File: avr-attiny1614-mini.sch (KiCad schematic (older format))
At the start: 15 parts, among them J1 Conn_01x05, J2 Conn_01x07, J3 BAT_JST_PH, Q1 Q_PMOS_GSD, SW1 SW_SPST, U1 attiny1614

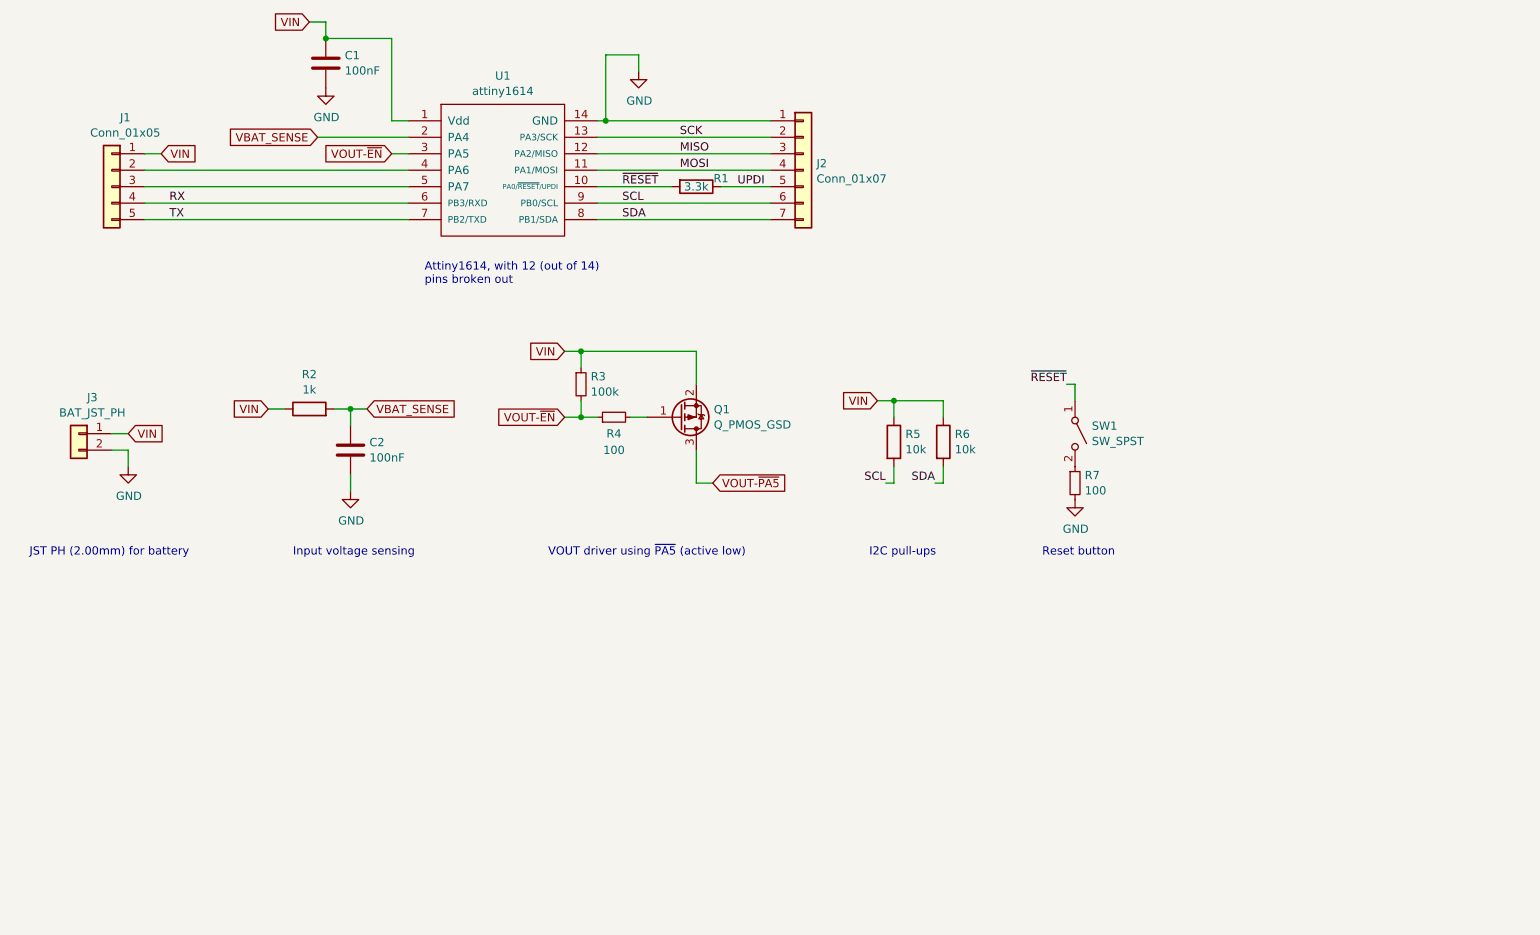
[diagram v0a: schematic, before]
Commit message: Remove VSENSE. Add EXT_LOAD driver.
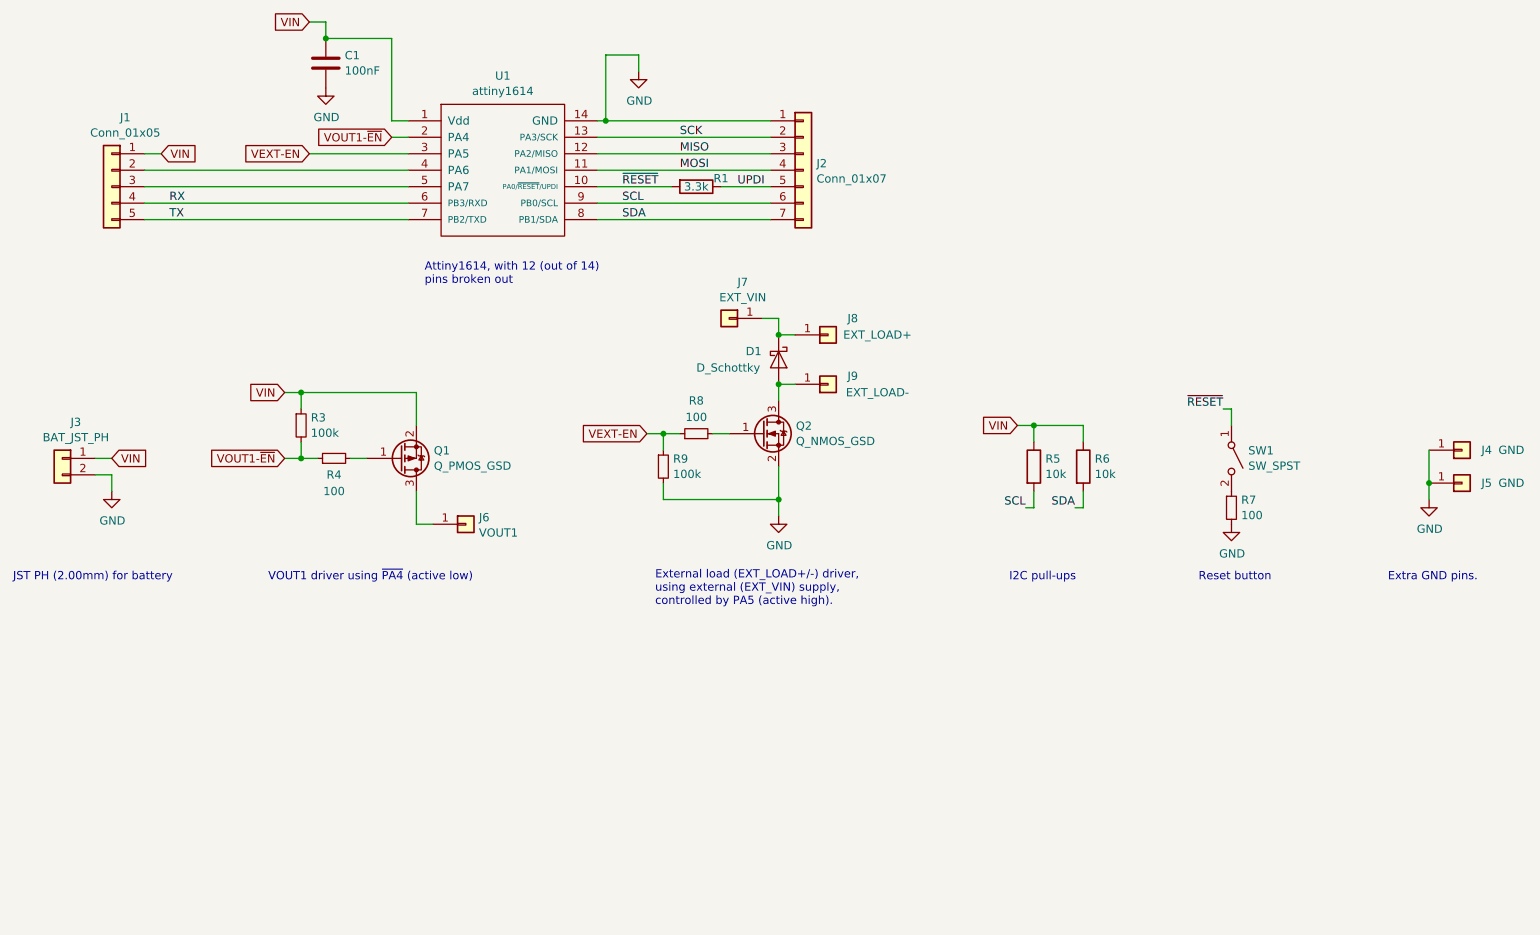
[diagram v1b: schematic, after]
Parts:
- removed C2: 100nF, local_footprints:0805_HS, symbol Device:C
- removed R2: 1k, local_footprints:0805_HS, symbol Device:R
- added D1: D_Schottky, local_footprints:1206_HS, symbol Device:D_Schottky
- added J4, J5: GND, local_footprints:Pin_Header_Straight_1x01_Pitch2.54mm, symbol Connector_Generic:Conn_01x01
- added J6: VOUT1, local_footprints:Pin_Header_Straight_1x01_Pitch2.54mm, symbol Connector_Generic:Conn_01x01
- added J7: EXT_VIN, local_footprints:Pin_Header_Straight_1x01_Pitch2.54mm, symbol Connector_Generic:Conn_01x01
- added J8: EXT_LOAD+, local_footprints:Pin_Header_Straight_1x01_Pitch2.54mm, symbol Connector_Generic:Conn_01x01
- added J9: EXT_LOAD-, local_footprints:Pin_Header_Straight_1x01_Pitch2.54mm, symbol Connector_Generic:Conn_01x01
- added Q2: Q_NMOS_GSD, local_footprints:SOT-23_HS, symbol Device:Q_NMOS_GSD
- added R8: 100, local_footprints:1206_HS, symbol Device:R_Small
- added R9: 100k, local_footprints:0805_HS, symbol Device:R_Small
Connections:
- net GND: now also J4.1 (Pin_1), J5.1 (Pin_1), Q2.2 (S), R9.2
- net VBAT_SENSE renamed VOUT1-~EN
- net VOUT1-~EN: now also R3.2, R4.1
- removed net VOUT-~EN: R3.2, R4.1, U1.3 (PA5)
- net VOUT-~PA5: no longer names the net of Q1.3 (D)
- net VOUT-~PA5: now also J6.1 (Pin_1)
- new net: Q2.1 (G), R8.2
- new net: D1.2 (A), J9.1 (Pin_1), Q2.3 (D)
- new net: D1.1 (K), J7.1 (Pin_1), J8.1 (Pin_1)
- new net VEXT-EN: R8.1, R9.1, U1.3 (PA5)
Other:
- note added: "External load (EXT_LOAD+/-) driver,\nusing external (EXT_VIN) supply,\ncontrolled by PA5 (active high)."
- note added: "Extra GND pins."
- note added: "VOUT1 driver using ~PA4~ (active low)"
- note removed: "Input voltage sensing"
- note removed: "VOUT driver using ~PA5~ (active low)"
- moved on the sheet: J3, Q1, R3, R4, R5, R6, R7, SW1

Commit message: Add micro USB for power
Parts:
- added J10: USB_B_Micro, local_footprints:USB-micro-B_Amphenol-10118194-0X0XLF_HS, symbol Connector:USB_B_Micro
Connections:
- net GND: now also J10.5 (GND)
- net VIN: now also J10.1 (VBUS)
- no-connect marks 0 -> 2
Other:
- note added: "Micro-USB connector for VIN."
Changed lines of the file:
@@
 Text Notes 9300 4900 0    50   ~ 0
 Extra GND pins.
+$Comp
+L Connector:USB_B_Micro J10
+U 1 1 5C15786E
+P 1400 5900
+F 0 "J10" H 1457 6370 50  0000 C CNN
+F 1 "USB_B_Micro" H 1457 6277 50  0000 C CNN
+F 2 "local_footprints:USB-micro-B_Amphenol-10118194-0X0XLF_HS" H 1550 5850 50  0001 C CNN
+F 3 "~" H 1550 5850 50  0001 C CNN
+	1    1400 5900
+	1    0    0    -1
+$EndComp
+Wire Wire Line
+	1400 6300 1400 6500
+$Comp
+L power:GND #PWR0101
+U 1 1 5C158E1E
+P 1400 6500
+F 0 "#PWR0101" H 1400 6250 50  0001 C CNN
+F 1 "GND" H 1404 6321 50  0000 C CNN
+F 2 "" H 1400 6500 50  0001 C CNN
+F 3 "" H 1400 6500 50  0001 C CNN
+	1    1400 6500
+	1    0    0    -1
+$EndComp
+Wire Wire Line
+	1700 5700 1900 5700
+Text GLabel 1900 5700 2    50   Input ~ 0
+VIN
+NoConn ~ 1700 5900
+NoConn ~ 1700 6000
+Text Notes 950  6950 0    50   ~ 0
+Micro-USB connector for VIN.
 $EndSCHEMATC

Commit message: Remove micro USB; minor tunings
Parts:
- removed J10: USB_B_Micro, local_footprints:USB-micro-B_Amphenol-10118194-0X0XLF_HS, symbol Connector:USB_B_Micro
- D1: footprint local_footprints:1206_HS -> local_footprints:1206_Diode_HS
- Q1: value Q_PMOS_GSD -> DMP2035U
- Q2: value Q_NMOS_GSD -> NTR3C21NZ
- R8: value 100 -> 1k; footprint local_footprints:1206_HS -> local_footprints:0805_HS
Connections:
- no-connect marks 2 -> 0
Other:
- note removed: "Micro-USB connector for VIN."
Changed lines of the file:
@@
 P 3300 4150
 F 0 "Q1" H 3506 4103 50  0000 L CNN
-F 1 "Q_PMOS_GSD" H 3506 4196 50  0000 L CNN
+F 1 "DMP2035U" H 3506 4196 50  0000 L CNN
 F 2 "local_footprints:SOT-23_HS" H 3500 4250 50  0001 C CNN
 F 3 "~" H 3300 4150 50  0001 C CNN
@@
 P 5500 4000
 F 0 "Q2" H 5705 4047 50  0000 L CNN
-F 1 "Q_NMOS_GSD" H 5705 3954 50  0000 L CNN
+F 1 "NTR3C21NZ" H 5705 3954 50  0000 L CNN
 F 2 "local_footprints:SOT-23_HS" H 5700 4100 50  0001 C CNN
 F 3 "~" H 5500 4000 50  0001 C CNN
@@
 P 5100 4000
 F 0 "R8" V 5300 4000 50  0000 C CNN
-F 1 "100" V 5200 4000 50  0000 C CNN
-F 2 "local_footprints:1206_HS" H 5100 4000 50  0001 C CNN
+F 1 "1k" V 5200 4000 50  0000 C CNN
+F 2 "local_footprints:0805_HS" H 5100 4000 50  0001 C CNN
 F 3 "~" H 5100 4000 50  0001 C CNN
 	1    5100 4000
@@
 F 0 "D1" V 5550 3350 50  0000 L CNN
 F 1 "D_Schottky" V 5650 3050 50  0000 L CNN
-F 2 "local_footprints:1206_HS" H 5600 3550 50  0001 C CNN
+F 2 "local_footprints:1206_Diode_HS" H 5600 3550 50  0001 C CNN
 F 3 "~" H 5600 3550 50  0001 C CNN
 	1    5600 3550
@@
 Text Notes 9300 4900 0    50   ~ 0
 Extra GND pins.
-$Comp
-L Connector:USB_B_Micro J10
-U 1 1 5C15786E
-P 1400 5900
-F 0 "J10" H 1457 6370 50  0000 C CNN
-F 1 "USB_B_Micro" H 1457 6277 50  0000 C CNN
-F 2 "local_footprints:USB-micro-B_Amphenol-10118194-0X0XLF_HS" H 1550 5850 50  0001 C CNN
-F 3 "~" H 1550 5850 50  0001 C CNN
-	1    1400 5900
-	1    0    0    -1
-$EndComp
-Wire Wire Line
-	1400 6300 1400 6500
-$Comp
-L power:GND #PWR0101
-U 1 1 5C158E1E
-P 1400 6500
-F 0 "#PWR0101" H 1400 6250 50  0001 C CNN
-F 1 "GND" H 1404 6321 50  0000 C CNN
-F 2 "" H 1400 6500 50  0001 C CNN
-F 3 "" H 1400 6500 50  0001 C CNN
-	1    1400 6500
-	1    0    0    -1
-$EndComp
-Wire Wire Line
-	1700 5700 1900 5700
-Text GLabel 1900 5700 2    50   Input ~ 0
-VIN
-NoConn ~ 1700 5900
-NoConn ~ 1700 6000
-Text Notes 950  6950 0    50   ~ 0
-Micro-USB connector for VIN.
 $EndSCHEMATC

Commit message: Layout exploring
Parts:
- removed J2: Conn_01x07, local_footprints:Pin_Header_Straight_1x07_Pitch2.54mm, symbol Connector_Generic:Conn_01x07
- added J10: UPDI, local_footprints:Pin_Header_Straight_1x01_Pitch2.54mm, symbol Connector_Generic:Conn_01x01
- added J2: Conn_01x06, local_footprints:Pin_Header_Straight_1x06_Pitch2.54mm, symbol Connector_Generic:Conn_01x06
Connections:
- net GND: now also J2.1 (Pin_1)
- net MISO: now also J2.3 (Pin_3)
- net MOSI: now also J2.4 (Pin_4)
- net SCK: now also J2.2 (Pin_2)
- net SCL: now also J2.5 (Pin_5)
- net SDA: now also J2.6 (Pin_6)
- net UPDI: now also J10.1 (Pin_1)
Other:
- note added: "UPDI prog header"
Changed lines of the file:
@@
 	0    1    1    0
 $EndComp
-$Comp
-L Connector_Generic:Conn_01x07 J2
-U 1 1 5C0C959B
-P 5750 2400
-F 0 "J2" H 5830 2441 50  0000 L CNN
-F 1 "Conn_01x07" H 5830 2348 50  0000 L CNN
-F 2 "local_footprints:Pin_Header_Straight_1x07_Pitch2.54mm" H 5750 2400 50  0001 C CNN
-F 3 "~" H 5750 2400 50  0001 C CNN
-	1    5750 2400
-	1    0    0    -1
-$EndComp
-Wire Wire Line
-	4500 2200 5550 2200
-Wire Wire Line
-	4500 2300 5550 2300
-Wire Wire Line
-	4500 2400 5550 2400
-Wire Wire Line
-	4500 2600 5550 2600
-Wire Wire Line
-	4500 2700 5550 2700
 Text Label 4650 2600 0    50   ~ 0
 SCL
@@
 	4750 1700 4750 1800
 Connection ~ 4550 2100
-Wire Wire Line
-	4550 2100 5550 2100
 $Comp
 L power:GND #PWR01
@@
 Wire Wire Line
 	4500 2500 4950 2500
-Wire Wire Line
-	5250 2500 5550 2500
-Text Label 5350 2500 0    50   ~ 0
-UPDI
 Text Notes 3450 3100 0    50   ~ 0
 Attiny1614, with 12 (out of 14)\npins broken out
@@
 Text Notes 9300 4900 0    50   ~ 0
 Extra GND pins.
+$Comp
+L Connector_Generic:Conn_01x06 J2
+U 1 1 5C0FA426
+P 5950 2300
+F 0 "J2" H 6030 2291 50  0000 L CNN
+F 1 "Conn_01x06" H 6030 2198 50  0000 L CNN
+F 2 "local_footprints:Pin_Header_Straight_1x06_Pitch2.54mm" H 5950 2300 50  0001 C CNN
+F 3 "~" H 5950 2300 50  0001 C CNN
+	1    5950 2300
+	1    0    0    -1
+$EndComp
+Wire Wire Line
+	5250 2500 5350 2500
+Text GLabel 5350 2500 2    50   Input ~ 0
+UPDI
+Wire Wire Line
+	4550 2100 5750 2100
+Wire Wire Line
+	4500 2200 5750 2200
+Wire Wire Line
+	4500 2300 5750 2300
+Wire Wire Line
+	4500 2400 5750 2400
+Wire Wire Line
+	5650 2600 5650 2500
+Wire Wire Line
+	5650 2500 5750 2500
+Wire Wire Line
+	4500 2600 5650 2600
+Wire Wire Line
+	5750 2700 5750 2600
+Wire Wire Line
+	4500 2700 5750 2700
+$Comp
+L Connector_Generic:Conn_01x01 J10
+U 1 1 5C1067D4
+P 7500 2500
+F 0 "J10" H 7650 2500 50  0000 C CNN
+F 1 "UPDI" H 7700 2400 50  0000 C CNN
+F 2 "local_footprints:Pin_Header_Straight_1x01_Pitch2.54mm" H 7500 2500 50  0001 C CNN
+F 3 "~" H 7500 2500 50  0001 C CNN
+	1    7500 2500
+	1    0    0    1
+$EndComp
+Text GLabel 7200 2500 0    50   Input ~ 0
+UPDI
+Wire Wire Line
+	7200 2500 7300 2500
+Text Notes 7000 2800 0    50   ~ 0
+UPDI prog header
 $EndSCHEMATC

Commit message: Approx placement for 1.2in x 0.6in board.
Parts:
- added J11: GND, local_footprints:Pin_Header_Straight_1x01_Pitch2.54mm, symbol Connector_Generic:Conn_01x01
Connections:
- net GND: now also J11.1 (Pin_1)
- net VOUT1: now reaches J6.1 (Pin_1), Q1.3 (D)
- net EXT_LOAD-: now reaches D1.2 (A), J9.1 (Pin_1), Q2.3 (D)
- net EXT_VIN_LOAD+: now reaches D1.1 (K), J7.1 (Pin_1), J8.1 (Pin_1)
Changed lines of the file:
@@
 U 1 1 5C1299A2
 P 5900 3400
-F 0 "J8" H 6050 3300 50  0000 C CNN
-F 1 "EXT_LOAD+" H 6200 3400 50  0000 C CNN
+F 0 "J8" H 6050 3350 50  0000 C CNN
+F 1 "EXT_LOAD+" H 6200 3450 50  0000 C CNN
 F 2 "local_footprints:Pin_Header_Straight_1x01_Pitch2.54mm" H 5900 3400 50  0001 C CNN
 F 3 "~" H 5900 3400 50  0001 C CNN
@@
 Text Notes 7000 2800 0    50   ~ 0
 UPDI prog header
+Text Label 5550 3300 0    50   ~ 0
+EXT_VIN_LOAD+
+Text Label 5600 3750 2    50   ~ 0
+EXT_LOAD-
+Text Label 3400 4550 2    50   ~ 0
+VOUT1
+$Comp
+L Connector_Generic:Conn_01x01 J11
+U 1 1 5C109BD6
+P 9750 3900
+F 0 "J11" H 9900 3900 50  0000 C CNN
+F 1 "GND" H 10050 3900 50  0000 C CNN
+F 2 "local_footprints:Pin_Header_Straight_1x01_Pitch2.54mm" H 9750 3900 50  0001 C CNN
+F 3 "~" H 9750 3900 50  0001 C CNN
+	1    9750 3900
+	1    0    0    1
+$EndComp
+Wire Wire Line
+	9550 3900 9550 4100
+Connection ~ 9550 4100
 $EndSCHEMATC
